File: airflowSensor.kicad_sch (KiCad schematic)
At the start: 5 parts, among them IC1 FS3000-1015

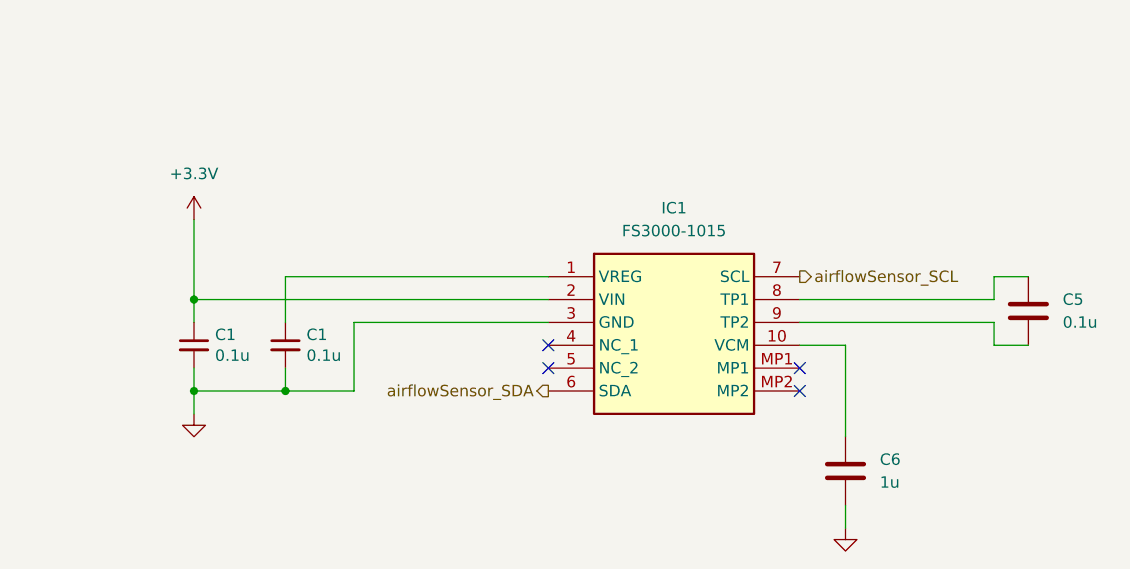
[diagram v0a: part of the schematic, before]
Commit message: temperatureSensor fix
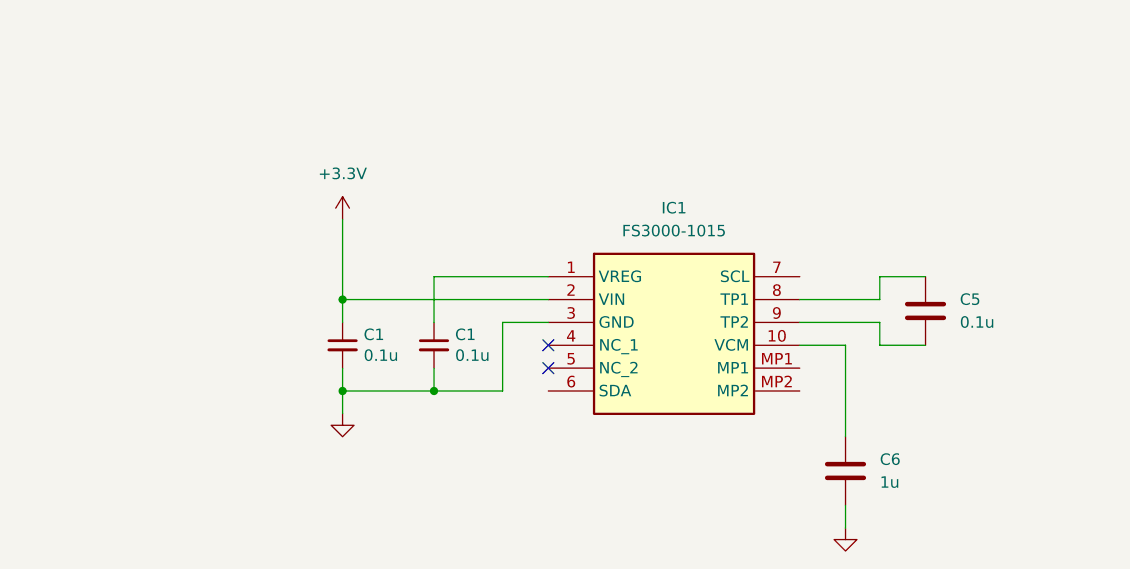
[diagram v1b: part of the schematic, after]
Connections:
- net airflowSensor_SCL: no longer names the net of IC1.7 (SCL)
- net airflowSensor_SDA: no longer names the net of IC1.6 (SDA)
- no-connect marks 4 -> 2
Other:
- moved on the sheet: C1, C5
